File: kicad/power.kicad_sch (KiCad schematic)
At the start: 64 parts, among them Q3 CSD17308Q3, Q4 CSD17308Q3, Q7 CSD17308Q3, Q8 CSD17308Q3, U17 LTC3856, U3 AP3211, U4 +0V8, U5 MCP1824T-1802E, U6 MCP1824T-0802E

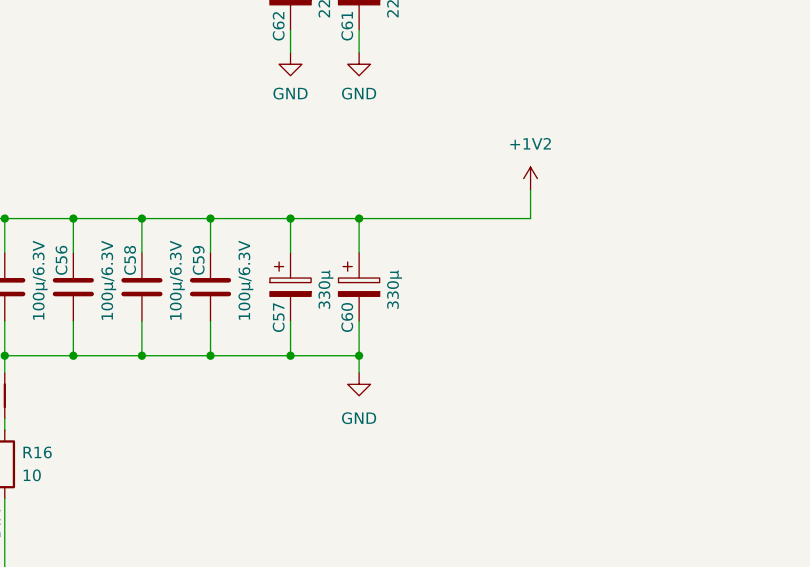
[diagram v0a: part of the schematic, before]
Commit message: replaced caps
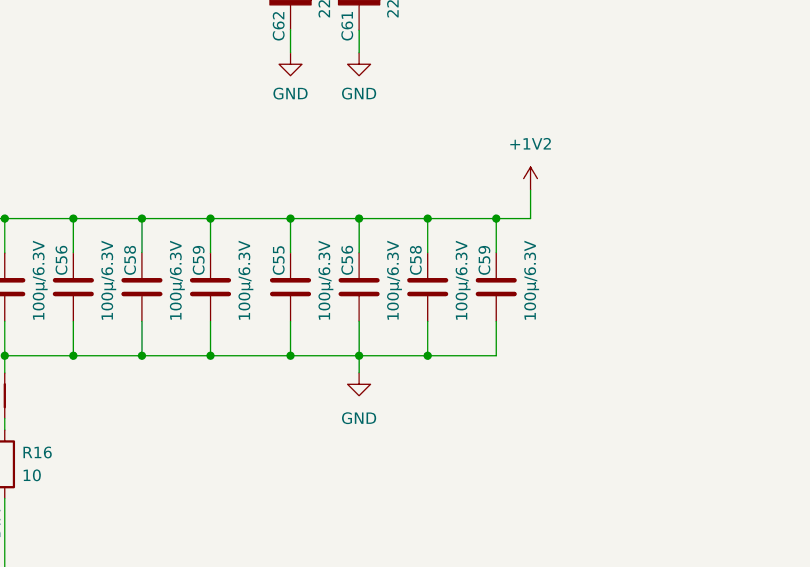
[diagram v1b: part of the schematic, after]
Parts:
- removed C57, C60: 330µ, Capacitor_SMD:CP_Elec_5x5.8, symbol Device:C_Polarized
- added C55, C56, C58, C59: 100µ/6.3V, Capacitor_SMD:C_1210_3225Metric, symbol Device:C
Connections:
- net +1V2: now also C55.1, C56.1, C58.1, C59.1
- net GND: now also C55.2, C56.2, C58.2, C59.2

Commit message: updated gerber, bom
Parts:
- removed C61, C62: 220µ, Capacitor_SMD:CP_Elec_5x5.8, symbol Device:C_Polarized
- added C55 (x4): 22µ/25V, Capacitor_SMD:C_1210_3225Metric, symbol Device:C
- added C95: 220µ/25V, Capacitor_SMD:CP_Elec_8x10, symbol Device:C_Polarized
- added R25: 49.9k, Resistor_SMD:R_0805_2012Metric, symbol Device:R
- added TP2 (x2): 3V3, TestPoint:TestPoint_Pad_2.0x2.0mm, symbol Connector:TestPoint
- C22, C23: PARTNO 0402X104K100CT -> (none)
- C24, C25: PARTNO EMK105BJ105MV-F -> (none)
- C54: value 4.7µ -> 4.7µ/25V
- D4, D5: value D_Schottky_Small -> CMDSH-3; Distributor (none) -> D; Manufacturer (none) -> CMDSH-3 TR PBFREE; OrderNr (none) -> 1514-CMDSH-3TRPBFREECT-ND
- D9: Distributor (none) -> D; Manufacturer (none) -> PMEG4030EP,115; OrderNr (none) -> 1727-5841-1-ND
- NT1, NT2, NT3, NT4: Distributor (none) -> -
- Q3, Q4, Q7, Q8: value CSD17308Q3 -> CSD16415Q5T; Manufacturer CSD17308Q3 -> CSD16415Q5T; OrderNr 296-27210-1-ND -> 296-49598-1-ND
- R31: footprint Resistor_SMD:R_2010_5025Metric -> Resistor_SMD:R_1206_3216Metric
- R5, R7: value 0.001 -> 1mR; Distributor (none) -> D; Manufacturer (none) -> TLR2HWDTE1L00F50; OrderNr (none) -> 2019-TLR2HWDTE1L00F50CT-ND
- U17: Distributor (none) -> D; Manufacturer (none) -> LTC3856EUH#PBF; OrderNr (none) -> LTC3856EUH#PBF-ND
- U3: Distributor (none) -> D; Manufacturer (none) -> AP3211KTR-G1; OrderNr (none) -> AP3211KTR-G1DICT-ND
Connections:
- net +12V: now also C55.1, C55.1, C55.1, C55.1, C95.1
- net +1V2: now also TP2.1
- net GND: now also C55.2, C55.2, C55.2, C55.2, C95.2, R25.1, TP2.1
- new net: R25.2, U17.12 (ISET)
- no-connect marks 3 -> 9
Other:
- moved on the sheet: C65
